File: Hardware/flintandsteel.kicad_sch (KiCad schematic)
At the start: 37 parts, among them J1 RBUS, U1 ESP32-S3, Y1 40MHz±10ppm

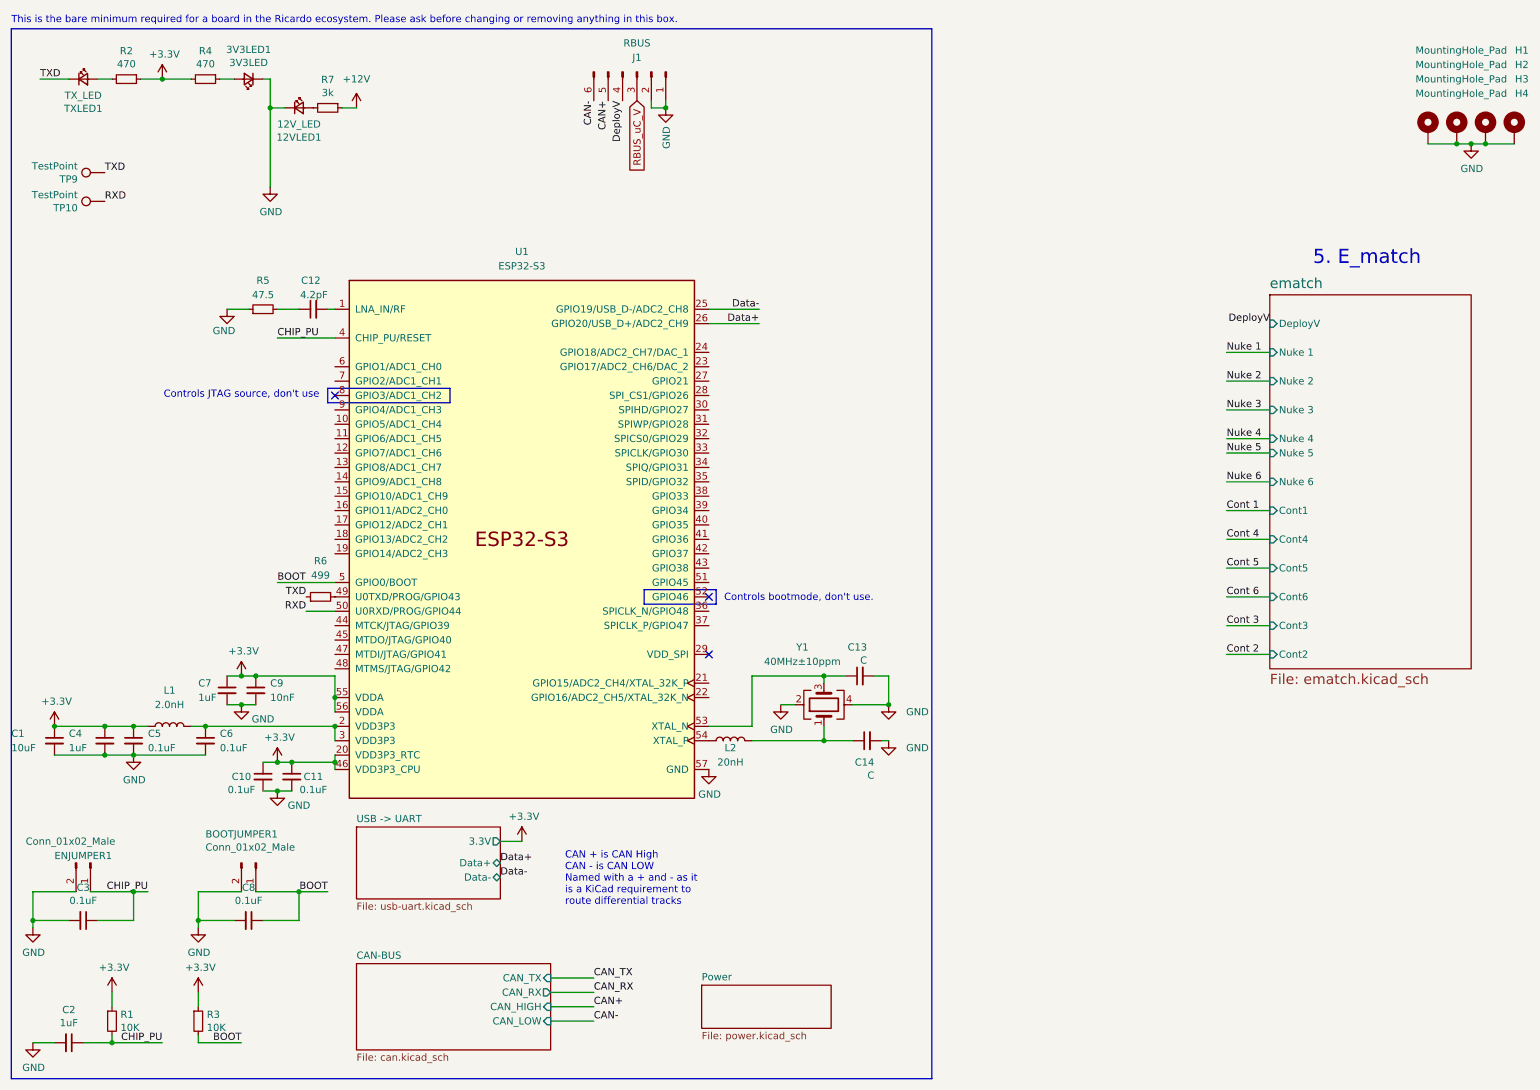
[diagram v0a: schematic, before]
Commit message: schematic done? + footprints assigned
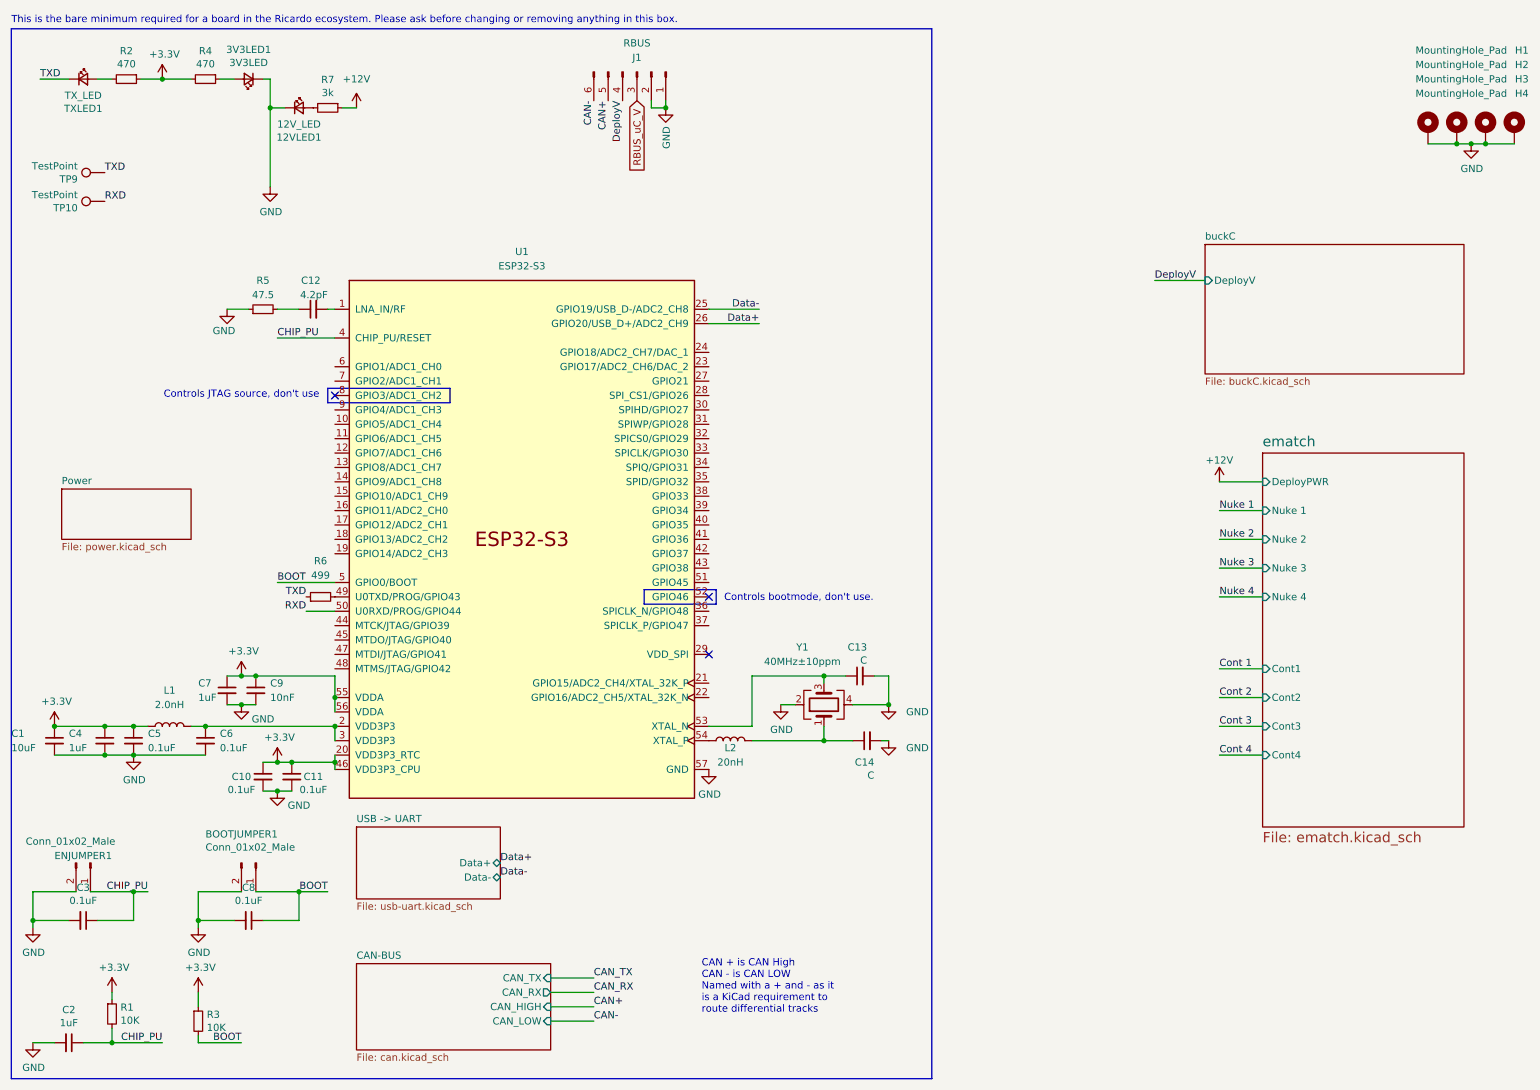
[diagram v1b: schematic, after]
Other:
- added sheet buckC (buckC.kicad_sch)
- sheet USB -> UART ports: added none; removed 3.3V
- sheet ematch ports: added DeployPWR; removed Cont5, Cont6, DeployV, Nuke 5, Nuke 6
- note removed: "5. E_match"
- moved on the sheet: R1

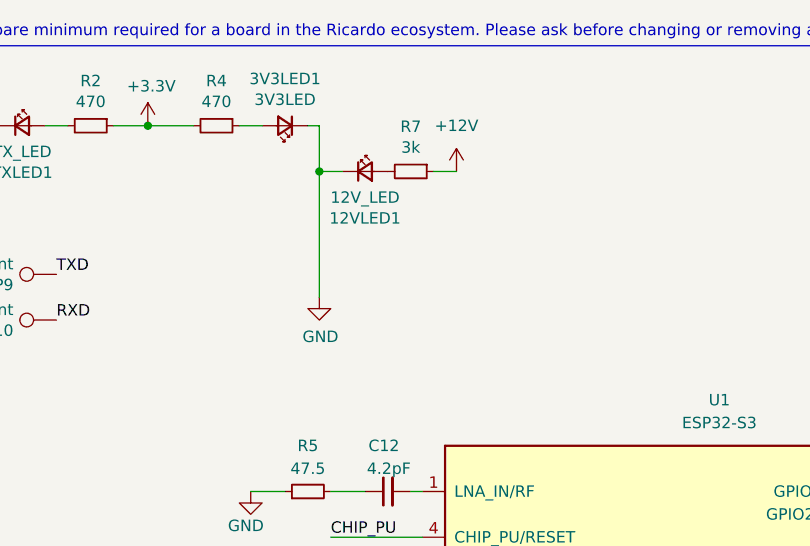
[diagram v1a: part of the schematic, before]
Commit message: started pyro channel layout
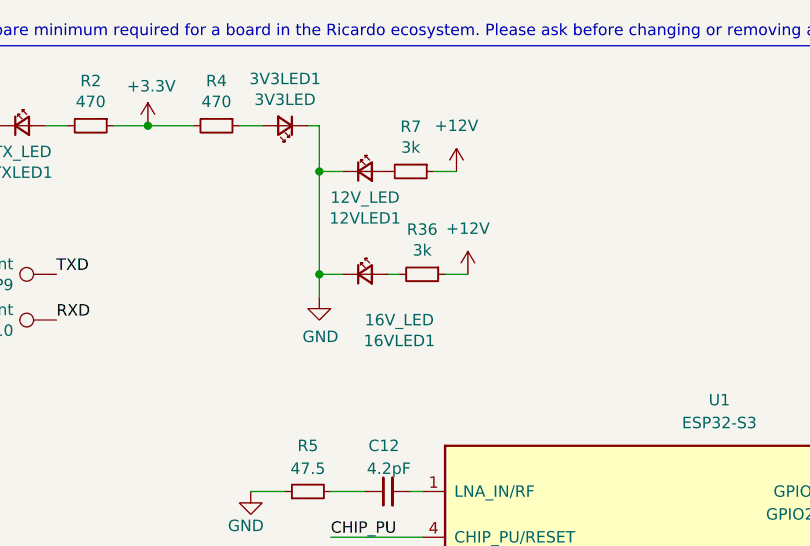
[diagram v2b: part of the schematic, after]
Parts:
- added 16VLED1: 16V_LED, Resistor_SMD:R_0402_1005Metric, symbol Device:LED_Small
- added R36: 3k, Resistor_SMD:R_0402_1005Metric, symbol Device:R_Small
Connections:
- net +12V: now also R36.1
- net GND: now also 16VLED1.1 (K)
- new net: 16VLED1.2 (A), R36.2
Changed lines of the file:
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@@
   (junction (at 30.48 191.77) (diameter 0) (color 0 0 0 0)
+  )
+  (junction (at 58.42 38.1) (diameter 0) (color 0 0 0 0)
   )
   (junction (at 69.85 142.24) (diameter 0) (color 0 0 0 0)
@@
     (stroke (width 0) (type default))
   )
+  (wire (pts (xy 58.42 38.1) (xy 58.42 40.64))
+    (stroke (width 0) (type default))
+  )
   (wire (pts (xy 69.85 135.89) (xy 69.85 138.43))
     (stroke (width 0) (type default))
@@
     (stroke (width 0) (type default))
   )
+  (wire (pts (xy 67.31 38.1) (xy 66.04 38.1))
+    (stroke (width 0) (type default))
+  )
   (wire (pts (xy 226.06 130.81) (xy 233.68 130.81))
     (stroke (width 0) (type default))
@@
     (stroke (width 0) (type default))
   )
+  (wire (pts (xy 60.96 38.1) (xy 58.42 38.1))
+    (stroke (width 0) (type default))
+  )
   (wire (pts (xy 226.06 107.95) (xy 233.68 107.95))
     (stroke (width 0) (type default))
@@
     (stroke (width 0) (type default))
   )
+  (wire (pts (xy 74.93 38.1) (xy 72.39 38.1))
+    (stroke (width 0) (type default))
+  )
   (wire (pts (xy 53.34 191.77) (xy 45.72 191.77))
     (stroke (width 0) (type default))
   )
-  (wire (pts (xy 58.42 26.67) (xy 58.42 40.64))
+  (wire (pts (xy 58.42 26.67) (xy 58.42 38.1))
     (stroke (width 0) (type default))
   )
@@
     )
   )
+  (symbol (lib_id "Device:LED_Small") (at 63.5 38.1 0) (unit 1)
+    (in_bom yes) (on_board yes) (dnp no)
+    (property "Reference" "16VLED1" (at 67.31 45.4914 0)
+      (effects (font (size 1.27 1.27)))
+    )
+    (property "Value" "16V_LED" (at 67.31 43.18 0)
+      (effects (font (size 1.27 1.27)))
+    )
+    (property "Footprint" "Resistor_SMD:R_0402_1005Metric" (at 63.5 38.1 90)
+      (effects (font (size 1.27 1.27)) hide)
+    )
+    (property "Datasheet" "~" (at 63.5 38.1 90)
+      (effects (font (size 1.27 1.27)) hide)
+    )
+    (pin "1")
+    (pin "2")
+    (instances
+      (project "flintandsteel"
+        (path "/7db990e4-92e1-4f99-b4d2-435bbec1ba83"
+          (reference "16VLED1") (unit 1)
+        )
+      )
+    )
+  )
   (symbol (lib_id "Mechanical:MountingHole_Pad") (at 267.97 30.48 0) (unit 1)
     (in_bom yes) (on_board yes) (dnp no)
@@
         (path "/7db990e4-92e1-4f99-b4d2-435bbec1ba83"
           (reference "L2") (unit 1)
+        )
+      )
+    )
+  )
+  (symbol (lib_id "Device:R_Small") (at 69.85 38.1 270) (unit 1)
+    (in_bom yes) (on_board yes) (dnp no)
+    (property "Reference" "R36" (at 69.85 33.1216 90)
+      (effects (font (size 1.27 1.27)))
+    )
+    (property "Value" "3k" (at 69.85 35.433 90)
+      (effects (font (size 1.27 1.27)))
+    )
+    (property "Footprint" "Resistor_SMD:R_0402_1005Metric" (at 69.85 38.1 0)
+      (effects (font (size 1.27 1.27)) hide)
+    )
+    (property "Datasheet" "~" (at 69.85 38.1 0)
+      (effects (font (size 1.27 1.27)) hide)
+    )
+    (pin "1")
+    (pin "2")
+    (instances
+      (project "flintandsteel"
+        (path "/7db990e4-92e1-4f99-b4d2-435bbec1ba83"
+          (reference "R36") (unit 1)
         )
       )
@@
         )
       )
+    )
+  )
+  (symbol (lib_id "power:+12V") (at 74.93 38.1 0) (unit 1)
+    (in_bom yes) (on_board yes) (dnp no)
+    (property "Reference" "#PWR083" (at 74.93 41.91 0)
+      (effects (font (size 1.27 1.27)) hide)
+    )
+    (property "Value" "+12V" (at 74.93 33.02 0)
+      (effects (font (size 1.27 1.27)))
+    )
+    (property "Footprint" "" (at 74.93 38.1 0)
+      (effects (font (size 1.27 1.27)) hide)
+    )
+    (property "Datasheet" "" (at 74.93 38.1 0)
+      (effects (font (size 1.27 1.27)) hide)
+    )
+    (pin "1")
+    (instances
+      (project "flintandsteel"
+        (path "/7db990e4-92e1-4f99-b4d2-435bbec1ba83"
+          (reference "#PWR083") (unit 1)
+        )
+      )

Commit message: I had to get back out of bed to push this commit
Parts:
- J1: footprint Connector_Molex:Molex_Mini-Fit_Jr_5566-06A_2x03_P4.20mm_Vertical -> Connector_Molex:Molex_Mini-Fit_Jr_5569-08A2_2x04_P4.20mm_Horizontal; symbol Connector:Conn_01x06_Male -> Connector:Conn_01x08_Pin
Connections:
- net CAN+: now also J1.7 (Pin_7); no longer J1.5 (Pin_5)
- net CAN-: now also J1.8 (Pin_8); no longer J1.6 (Pin_6)
- net DeployV: now also J1.5 (Pin_5), J1.6 (Pin_6); no longer J1.4 (Pin_4)
- net GND: now also J1.3 (Pin_3)
- net RBUS_uC_V: now also J1.4 (Pin_4); no longer J1.3 (Pin_3)
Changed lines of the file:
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@@
+    (stroke (width 0) (type default))
+  )
+  (wire (pts (xy 130.81 25.4) (xy 130.81 26.67))
     (stroke (width 0) (type default))
   )
@@
   )
   (wire (pts (xy 59.69 147.32) (xy 62.23 147.32))
+    (stroke (width 0) (type default))
+  )
+  (wire (pts (xy 130.81 26.67) (xy 128.27 26.67))
     (stroke (width 0) (type default))
   )
@@
     (effects (font (size 1.27 1.27)) (justify left bottom))
   )
+  (label "DeployV" (at 118.11 25.4 270) (fields_autoplaced)
+    (effects (font (size 1.27 1.27)) (justify right bottom))
+  )
   (label "Nuke 3" (at 226.06 107.95 0) (fields_autoplaced)
     (effects (font (size 1.27 1.27)) (justify left bottom))
@@
     (effects (font (size 1.27 1.27)) (justify left bottom))
   )
+  (label "CAN-" (at 113.03 25.4 270) (fields_autoplaced)
+    (effects (font (size 1.27 1.27)) (justify right bottom))
+  )
   (label "BOOT" (at 53.34 191.77 180) (fields_autoplaced)
     (effects (font (size 1.27 1.27)) (justify right bottom))
@@
     (effects (font (size 1.27 1.27)) (justify left bottom))
   )
-  (label "CAN-" (at 115.57 25.4 270) (fields_autoplaced)
-    (effects (font (size 1.27 1.27)) (justify right bottom))
-  )
-  (label "CAN+" (at 118.11 25.4 270) (fields_autoplaced)
-    (effects (font (size 1.27 1.27)) (justify right bottom))
-  )
   (label "CAN_TX" (at 115.57 180.34 0) (fields_autoplaced)
     (effects (font (size 1.27 1.27)) (justify left bottom))
@@
   )
   (label "TXD" (at 64.77 113.03 180) (fields_autoplaced)
+    (effects (font (size 1.27 1.27)) (justify right bottom))
+  )
+  (label "CAN+" (at 115.57 25.4 270) (fields_autoplaced)
     (effects (font (size 1.27 1.27)) (justify right bottom))
   )
@@
     )
   )
-  (symbol (lib_id "Connector:Conn_01x06_Male") (at 123.19 20.32 270) (unit 1)
+  (symbol (lib_id "Connector:Conn_01x08_Pin") (at 123.19 20.32 270) (unit 1)
     (in_bom yes) (on_board yes) (dnp no)
     (property "Reference" "J1" (at 123.19 17.78 90)
@@
       (effects (font (size 1.27 1.27)))
     )
-    (property "Footprint" "Connector_Molex:Molex_Mini-Fit_Jr_5566-06A_2x03_P4.20mm_Vertical" (at 123.19 20.32 0)
+    (property "Footprint" "Connector_Molex:Molex_Mini-Fit_Jr_5569-08A2_2x04_P4.20mm_Horizontal" (at 123.19 20.32 0)
       (effects (font (size 1.27 1.27)) hide)
     )
@@
     (pin "5")
     (pin "6")
-    (instances
-      (project "flintandsteel"
+    (pin "7")
+    (pin "8")
+    (instances
+      (project "flintandsteel"

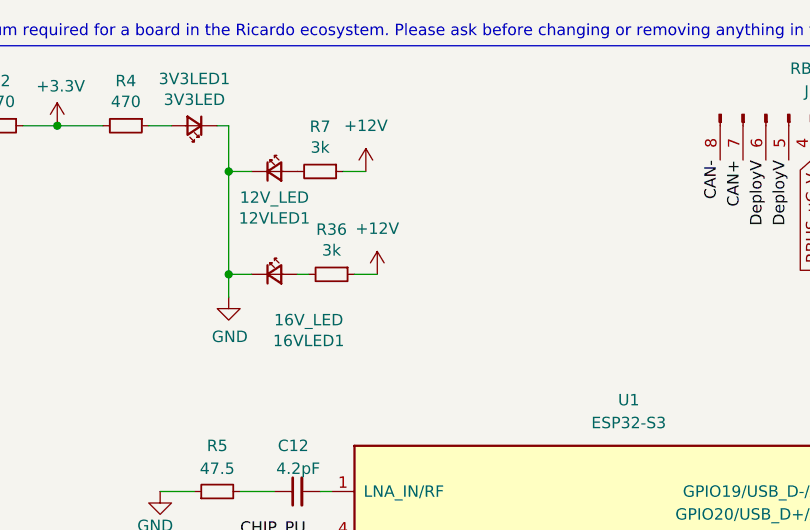
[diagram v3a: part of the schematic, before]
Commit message: high V side finished, CAN circuit and ESP left to place
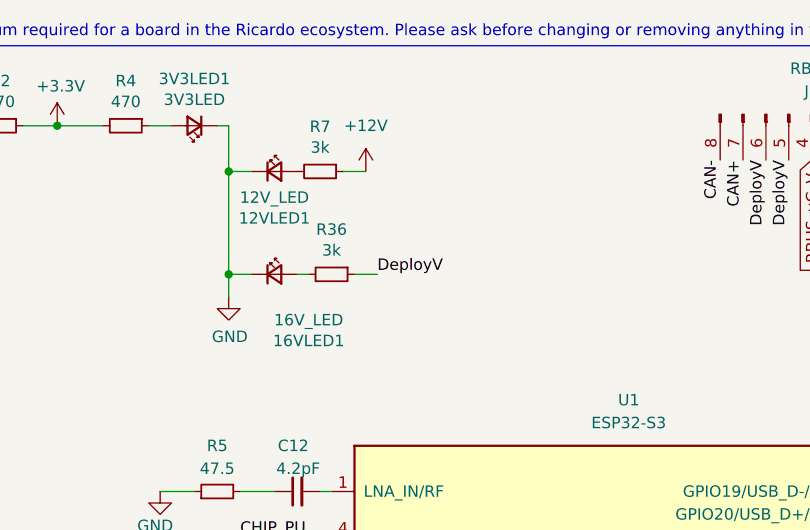
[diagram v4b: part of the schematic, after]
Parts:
- 12VLED1, 16VLED1, 3V3LED1: footprint Resistor_SMD:R_0402_1005Metric -> Diode_SMD:D_0402_1005Metric
- U1: footprint Package_DFN_QFN:QFN-56-1EP_7x7mm_P0.4mm_EP5.6x5.6mm -> iclr:QFN40P700X700X90-57N
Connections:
- net +12V: no longer R36.1
- net DeployV: now also R36.1
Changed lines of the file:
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@@
     (effects (font (size 1.27 1.27)) (justify right bottom))
+  )
+  (label "DeployV" (at 74.93 38.1 0) (fields_autoplaced)
+    (effects (font (size 1.27 1.27)) (justify left bottom))
   )
   (label "Cont 4" (at 226.06 140.97 0) (fields_autoplaced)
@@
       (effects (font (size 1.27 1.27)))
     )
-    (property "Footprint" "Resistor_SMD:R_0402_1005Metric" (at 54.61 21.59 90)
+    (property "Footprint" "Diode_SMD:D_0402_1005Metric" (at 54.61 21.59 90)
       (effects (font (size 1.27 1.27)) hide)
     )
@@
       (effects (font (size 1.27 1.27)))
     )
-    (property "Footprint" "Resistor_SMD:R_0402_1005Metric" (at 63.5 26.67 90)
+    (property "Footprint" "Diode_SMD:D_0402_1005Metric" (at 63.5 26.67 90)
       (effects (font (size 1.27 1.27)) hide)
     )
@@
       (effects (font (size 1.27 1.27)))
     )
-    (property "Footprint" "Resistor_SMD:R_0402_1005Metric" (at 63.5 38.1 90)
+    (property "Footprint" "Diode_SMD:D_0402_1005Metric" (at 63.5 38.1 90)
       (effects (font (size 1.27 1.27)) hide)
     )
@@
       (effects (font (size 1.27 1.27)))
     )
-    (property "Footprint" "Package_DFN_QFN:QFN-56-1EP_7x7mm_P0.4mm_EP5.6x5.6mm" (at 102.87 153.67 0)
+    (property "Footprint" "iclr:QFN40P700X700X90-57N" (at 102.87 153.67 0)
       (effects (font (size 1.27 1.27)) hide)
     )
@@
         )
       )
-    )
-  )
-  (symbol (lib_id "power:+12V") (at 74.93 38.1 0) (unit 1)
-    (in_bom yes) (on_board yes) (dnp no)
-    (property "Reference" "#PWR083" (at 74.93 41.91 0)
-      (effects (font (size 1.27 1.27)) hide)
-    )
-    (property "Value" "+12V" (at 74.93 33.02 0)
-      (effects (font (size 1.27 1.27)))
-    )
-    (property "Footprint" "" (at 74.93 38.1 0)
-      (effects (font (size 1.27 1.27)) hide)
-    )
-    (property "Datasheet" "" (at 74.93 38.1 0)
-      (effects (font (size 1.27 1.27)) hide)
-    )
-    (pin "1")
-    (instances
-      (project "flintandsteel"
-        (path "/7db990e4-92e1-4f99-b4d2-435bbec1ba83"
-          (reference "#PWR083") (unit 1)
-        )
-      )

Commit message: finished? (pre-review)
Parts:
- added R37: 1.5k, Resistor_SMD:R_0402_1005Metric, symbol Device:R_Small
- added R38: 2.2k, Resistor_SMD:R_0402_1005Metric, symbol Device:R_Small
- TXLED1: footprint Resistor_SMD:R_0402_1005Metric -> Diode_SMD:D_0402_1005Metric
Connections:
- net BOOT: now also BOOTJUMPER1.2 (Pin_2); no longer BOOTJUMPER1.1 (Pin_1)
- net CAN_RX: now also U1.23 (GPIO17/ADC2_CH6/DAC_2)
- net CAN_TX: now also U1.24 (GPIO18/ADC2_CH7/DAC_1)
- net CHIP_PU: now also ENJUMPER1.2 (Pin_2); no longer ENJUMPER1.1 (Pin_1)
- net Cont 1: now also U1.41 (GPIO36)
- net Cont 2: now also U1.37 (SPICLK_P/GPIO47)
- net Cont 3: now also U1.43 (GPIO38)
- net Cont 4: now also U1.42 (GPIO37)
- net GND: now also BOOTJUMPER1.1 (Pin_1), ENJUMPER1.1 (Pin_1), R38.1; no longer BOOTJUMPER1.2 (Pin_2), ENJUMPER1.2 (Pin_2)
- net Nuke 1: now also U1.40 (GPIO35)
- net Nuke 2: now also U1.39 (GPIO34)
- net Nuke 3: now also U1.38 (GPIO33)
- net Nuke 4: now also U1.27 (GPIO21)
- net BuckPGOOD: now reaches U1.15 (GPIO10/ADC1_CH9)
- net BuckPGOOD: now also R37.1, R38.2
- new net buckC/PGOOD: R37.2
- no-connect marks 3 -> 28
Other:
- sheet buckC ports: added PGOOD; removed none
- moved on the sheet: BOOTJUMPER1, ENJUMPER1
